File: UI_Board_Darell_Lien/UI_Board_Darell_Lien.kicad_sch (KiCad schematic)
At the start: 0 parts

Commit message: updated UI_Board_Darell_Lien
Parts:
- added A1: Adafruit_Feather_HUZZAH32_ESP32, Module:Adafruit_Feather, symbol MCU_Module:Adafruit_Feather_HUZZAH32_ESP32
- added B2: ~, SMV_Misc:Twidec Button, symbol SMV_Custom:Twidec_Button
- added C2: 0.33uf, symbol Device:C_Small
- added C3 (x2): 0.1uf, symbol Device:C_Small
- added C5, C6, C7: 10uf, symbol Device:C_Small
- added J1, J2: XT60-M, SMV_Connectors:AMASS_XT60-M, symbol SMV_Custom:XT60-M
- added Q1, Q2, Q3, Q4: PN2222A, Package_TO_SOT_THT:TO-92_Inline, symbol Transistor_BJT:PN2222A
- added R1, R2, R4: 120, symbol Device:R_US
- added R10, R11, R12, R13, R6, R7, R8, R9: 220, symbol Device:R_Small_US
- added R3: 10k-20k, symbol Device:R_Variable_US
- added R5: R_Small_US, symbol Device:R_Small_US
- added S1, S2, S3, S4, S5, S6: ~, SMV_Misc:TAISS 3 Pin Switch, symbol SMV_Custom:TAISS_3_Pin_Switch
- added SW1: A8L-11-12N1, SMV_Misc:SW_A8L-11_OMR, symbol SMV_Custom:A8L-11-12N1
- added U1: ~, symbol SMV_Custom:STM32_Nucleo_F446RE
- added U2: MCP2562-E-P, Package_DIP:DIP-8_W7.62mm, symbol Interface_CAN_LIN:MCP2562-E-P
- added U3: UA78M05QDCYRG4Q1, SMV_ICs:DCY4_TEX, symbol SMV_Custom:UA78M05QDCYRG4Q1
- added U4: ~, symbol SMV_Custom:NHD-0420AZ-FSW-GBW-33V3
- added U5: TPS7A2030PDBVR, DBV0005A-IPC_A, symbol SMV_Custom:TPS7A2030PDBVR
- added U6: ~, symbol SMV_Custom:Seven_Seg_Display
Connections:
- new net: R8.2, U6.9 (A)
- new net: R13.1, U6.1 (E)
- new net: R7.2, U6.10 (F)
- new net: R6.2, U6.11 (G)
- new net: Q1.3 (C), U6.12 (DIGIT_1)
- new net: R12.1, U6.2 (D)
- new net: Q4.3 (C), U6.3 (DIGIT_4)
- new net: R11.1, U6.4 (C)
- new net: R10.1, U6.5 (DP)
- new net: R9.1, U6.6 (B)
- new net: Q3.3 (C), U6.7 (DIGIT_3)
- new net: Q2.3 (C), U6.8 (DIGIT_2)
- new net 12v: C2.1, J1.P (POS), J2.P (POS), U3.3 (INPUT)
- new net 3v: C7.2, U4.15 (LED+), U5.5 (OUT)
- new net 3v3: A1.2 (3V3), B2.2, C5.1, R2.2, R3.2, R4.2, S1.1 (Top), S2.1 (Top), S3.1 (Top), S4.1 (Top), S5.1 (Top), S6.1 (Top), SW1.2, U1.16 (+3V3), U2.5 (Vio), U4.2 (VDD)
- new net 5v: C3.2, C3.2, C6.2, U1.6 (E5V), U2.3 (VDD), U3.1 (OUTPUT), U5.1 (IN), U5.3 (EN)
- new net CANH: R1.1, R5.1, U2.7 (CANH)
- new net CANL: R1.2, R5.2, U2.6 (CANL)
- new net GND: A1.4 (GND), C2.2, C3.1, C3.1, C5.2, C6.1, C7.1, J1.N (NEG), J2.N (NEG), Q1.1 (E), Q2.1 (E), Q3.1 (E), Q4.1 (E), R2.1, R3.1, R4.1, S1.3 (Bottom), S2.3 (Bottom), S3.3 (Bottom), S4.3 (Bottom), S5.3 (Bottom), S6.3 (Bottom), U1.19 (GND), U2.2 (VSS), U2.8 (STBY), U3.2 (GND), U3.4 (GND), U4.1 (VSS), U4.16 (LED-), U5.2 (GND)
- new net PA0: S1.2 (Center), U1.28 (PA0)
- new net PA1: S2.2 (Center), U1.30 (PA1)
- new net PA2: S3.2 (Center), U1.73 (PA2)
- new net PA3: S4.2 (Center), U1.75 (PA3)
- new net PA4: S5.2 (Center), U1.32 (PA4)
- new net PA5: S6.2 (Center), U1.49 (PA5)
- new net PA6: SW1.1, U1.51 (PA6)
- new net PA7: B2.1, U1.53 (PA7)
- new net PB0: Q1.2 (B), U1.34 (PB0)
- new net PB1: Q2.2 (B), U1.62 (PB1)
- new net PB10: R6.1, U1.63 (PB10)
- new net PB12: R10.2, U1.54 (PB12)
- new net PB2: Q3.2 (B), U1.60 (PB2)
- new net PB3: Q4.2 (B), U1.69 (PB3)
- new net PB4: R8.1, U1.65 (PB4)
- new net PB5: R9.2, U1.67 (PB5)
- new net PB6: R11.2, U1.55 (PB6)
- new net PB7: R12.2, U1.21 (PB7)
- new net PB8: R13.2, U1.41 (PB8)
- new net PB9: R7.1, U1.43 (PB9)
- new net RX: A1.14 (RX/IO16), U1.71 (PA10)
- new net RXD: U1.52 (PA11), U2.4 (RXD)
- new net TX: A1.15 (TX/IO17), U1.59 (PA9)
- new net TXD: U1.50 (PA12), U2.1 (TXD)

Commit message: updated schematic 1/5
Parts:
- removed R1: 120, symbol Device:R_US
- removed S6: ~, SMV_Misc:TAISS 3 Pin Switch, symbol SMV_Custom:TAISS_3_Pin_Switch
- added B1: ~, SMV_Misc:Twidec Button, symbol SMV_Custom:Twidec_Button
- added J3, J4: 22035035, SMV_Connectors:3pin_CON_22035035_MOL, symbol SMV_Custom:3-pin Mini Molex Spox
- added R1, R14, R16, R17, R18: 10k, symbol Device:R_Small_US
- added R15: 120, symbol Device:R_US
- added R19: 0, symbol Device:R_Small_US
- R5: value R_Small_US -> 10k
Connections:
- net CANH: now also J3.1, J4.1; no longer R5.1
- net CANL: now also J3.3, J4.3; no longer R5.2
- net GND: now also R5.1, U4.5 (R/W), J3.2, J4.2, R1.1, R14.1, R15.1, R16.1, R17.1, R18.1; no longer S4.3 (Bottom)
- net PA0: now also R5.2, S1.1 (Top); no longer S1.2 (Center), U1.28 (PA0)
- net PA1: now also S2.1 (Top), R14.2; no longer S2.2 (Center)
- net PA2: now also S3.1 (Top), R16.2; no longer S3.2 (Center)
- net PA3: now also S4.1 (Top), R17.2; no longer S4.2 (Center)
- net PA4: now also S5.1 (Top), R1.2; no longer S5.2 (Center)
- net PA5: now also S4.3 (Bottom), R18.2
- net PA6: now also R2.2
- net PA7: now also B1.1, R15.2; no longer B2.1
- net PB0: now also U1.28 (PA0)
- net at U1.33 (VBAT): now also R19.1
- net PC2: now reaches U1.35 (PC2)
- net PC2: now also U4.6 (E)
- net PC1: now reaches U1.36 (PC1)
- net PC1: now also U4.4 (RS)
- net PC3: now reaches U1.37 (PC3)
- net PC3: now also U4.11 (DB4)
- net PC0: now reaches U1.38 (PC0)
- net PC0: now also B2.1, R4.2
- net PC6: now reaches U1.42 (PC6)
- net PC6: now also U4.14 (DB7)
- net PC5: now reaches U1.44 (PC5)
- net PC5: now also U4.13 (DB6)
- net at U1.5 (VDD): now also R19.2
- net PC4: now reaches U1.72 (PC4)
- net PC4: now also U4.12 (DB5)
- net 12v renamed +12V
- net 3v renamed +3V0
- net 3v3 renamed +3V3
- net +3V3: now also S1.2 (Center), S2.2 (Center), S3.2 (Center), S4.2 (Center), S5.2 (Center), B1.2; no longer R2.2, R4.2, S1.1 (Top), S2.1 (Top), S3.1 (Top), S4.1 (Top), S5.1 (Top)
- net 5v renamed +5V
- no-connect marks 0 -> 62
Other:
- note added: "Emergency"
- note added: "Head Lights"
- note added: "Horn"
- note added: "Ignition"
- note added: "Left and Right Blinker"
- note added: "Regen"
- note added: "Supercaps"
- note added: "Wiper"
- moved on the sheet: A1, B2, R2, R4, S1, S2, S3, S4, S5, SW1

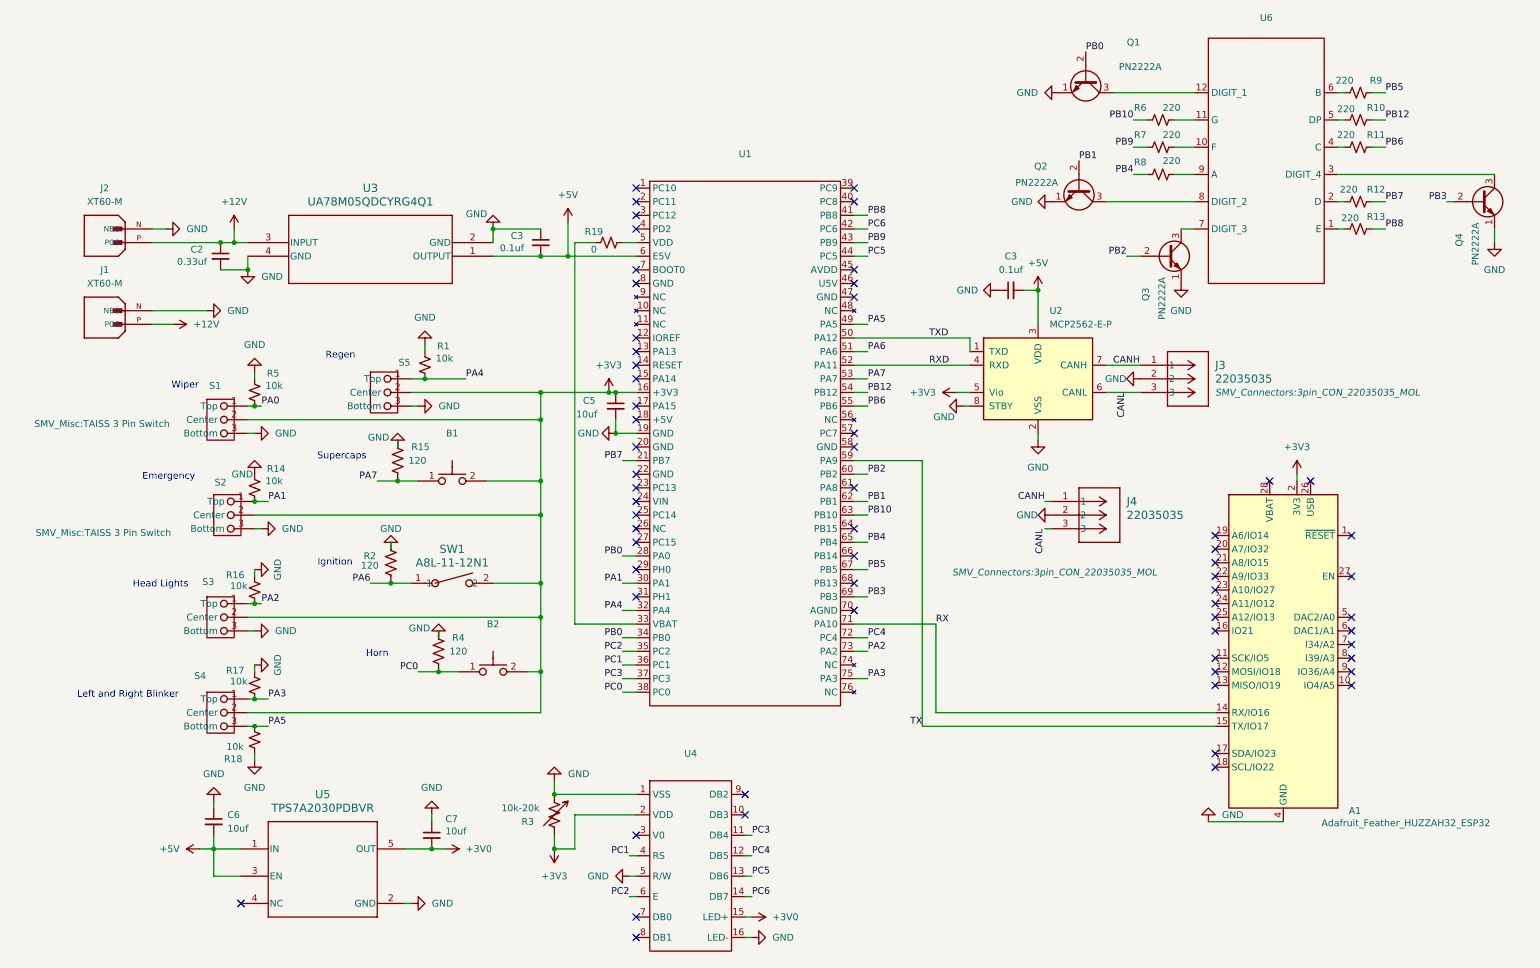
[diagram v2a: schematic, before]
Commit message: updated schematic 1/8
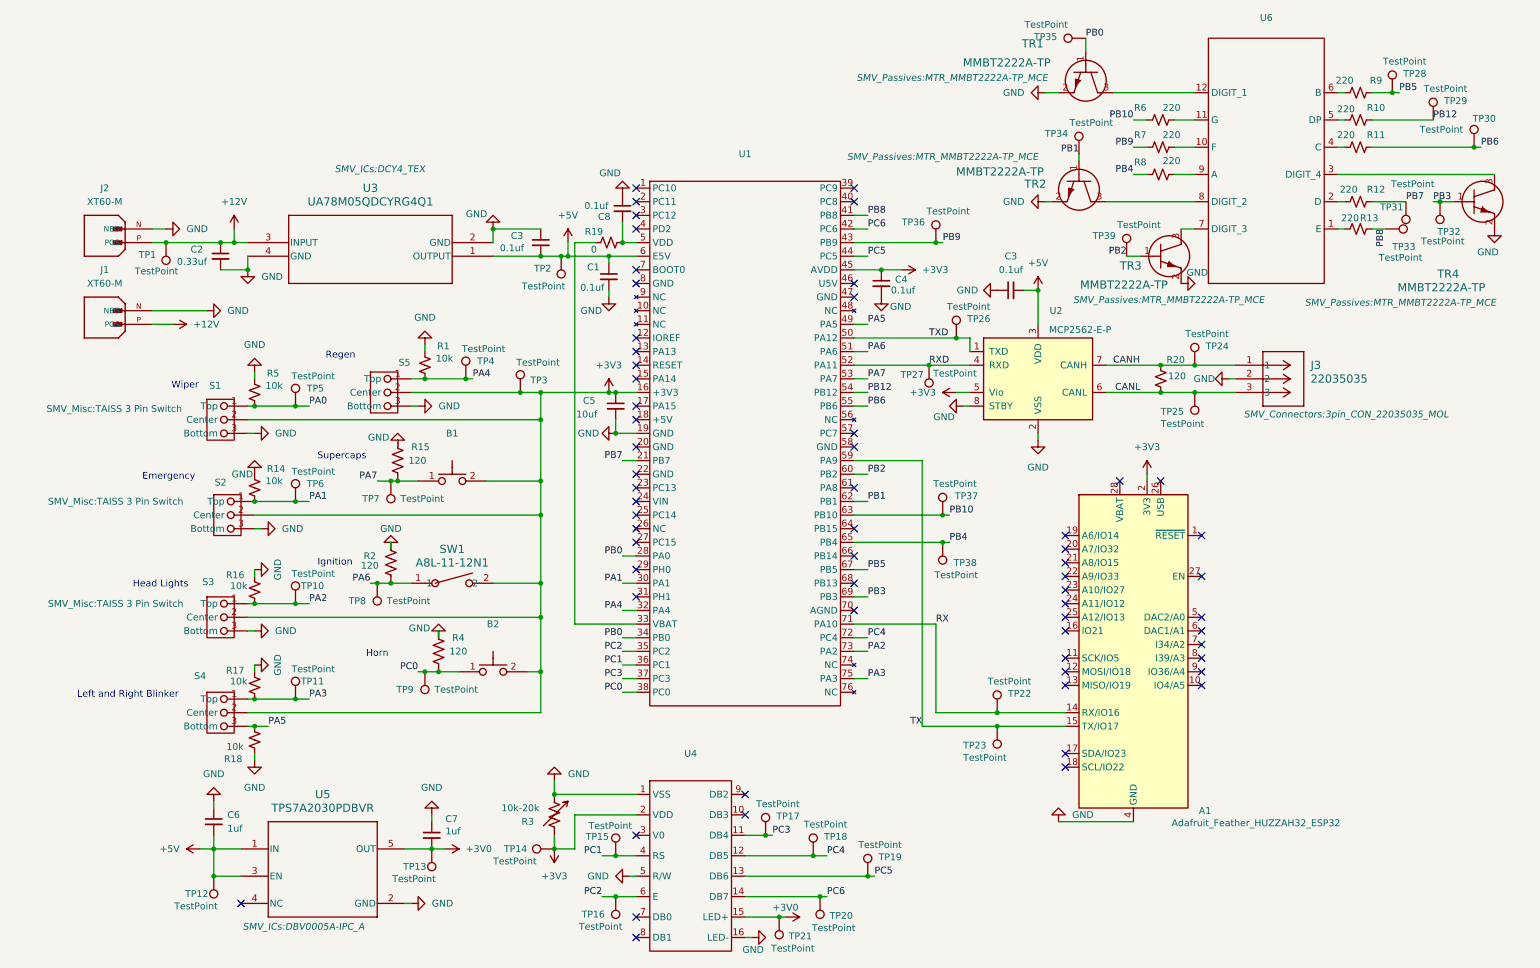
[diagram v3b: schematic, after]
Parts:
- removed J4: 22035035, SMV_Connectors:3pin_CON_22035035_MOL, symbol SMV_Custom:3-pin Mini Molex Spox
- removed Q1, Q2, Q3, Q4: PN2222A, Package_TO_SOT_THT:TO-92_Inline, symbol Transistor_BJT:PN2222A
- added C1, C4, C8: 0.1uf, symbol Device:C_Small
- added R20: 120, symbol Device:R_Small_US
- added TP1, TP10, TP11, TP12, TP13, TP14, TP15, TP16, TP17, TP18, TP19, TP2, TP20, TP21, TP22, TP23, TP24, TP25, TP26, TP27, TP28, TP29, TP3, TP30, TP31, TP32, TP33, TP34, TP35, TP36, TP37, TP38, TP39, TP4, TP5, TP6, TP7, TP8, TP9: TestPoint, symbol Connector:TestPoint
- added TR1, TR2, TR3, TR4: MMBT2222A-TP, SMV_Passives:MTR_MMBT2222A-TP_MCE, symbol SMV_Custom:MMBT2222A-TP
- C6, C7: value 10uf -> 1uf
- U5: footprint DBV0005A-IPC_A -> SMV_ICs:DBV0005A-IPC_A
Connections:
- net +12V: now also TP1.1
- net +3V0: now also TP13.1, TP21.1
- net +3V3: now also U1.45 (AVDD), C4.1, TP14.1, TP3.1
- net +5V: now also C1.1, TP12.1, TP2.1
- net CANH: now also R20.2, TP24.1
- net CANL: now also R20.1, TP25.1
- net GND: now also C1.2, C4.2, C8.1, TR1.2, TR2.2, TR3.2, TR4.2
- net PA0: now also TP5.1
- net PA1: now also TP6.1
- net PA2: now also TP10.1
- net PA3: now also TP11.1
- net PA4: now also TP4.1
- net PA6: now also TP8.1
- net PA7: now also TP7.1
- net PB0: now also TP35.1, TR1.1
- net PB1: now also TP34.1, TR2.1
- net PB10: now also TP37.1
- net PB12: now also TP29.1
- net PB2: now also TP39.1, TR3.1
- net PB3: now also TP32.1, TR4.1
- net PB4: now also TP38.1
- net PB5: now also TP28.1
- net PB6: now also TP30.1
- net PB7: now also TP31.1
- net PB8: now also TP33.1
- net PB9: now also TP36.1
- net PC0: now also TP9.1
- net PC1: now also TP15.1
- net PC2: now also TP16.1
- net PC3: now also TP17.1
- net PC4: now also TP18.1
- net PC5: now also TP19.1
- net PC6: now also TP20.1
- net RX: now also TP22.1
- net RXD: now also TP27.1
- net TX: now also TP23.1
- net TXD: now also TP26.1
- net at R19.2, U1.5 (VDD): now also C8.2
- net at U6.12 (DIGIT_1): now also TR1.3
- net at U6.3 (DIGIT_4): now also TR4.3
- net at U6.7 (DIGIT_3): now also TR3.3
- net at U6.8 (DIGIT_2): now also TR2.3
- no-connect marks 62 -> 61
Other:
- moved on the sheet: A1, J3
